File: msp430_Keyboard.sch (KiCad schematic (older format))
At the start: 26 parts, among them J1 Conn_01x04_Male, SW14 L_Super, SW4 L_Ctrl, SW48 R_Ctrl, SW5 L_Shift, SW53 R_Shift, SW57 Alt_GR, SW60 R_Super, SW61 FUNC, SW9 L_Alt, U1 MSP430F5510IRGZ, Y1 12MHz, Y2 32.768kHz

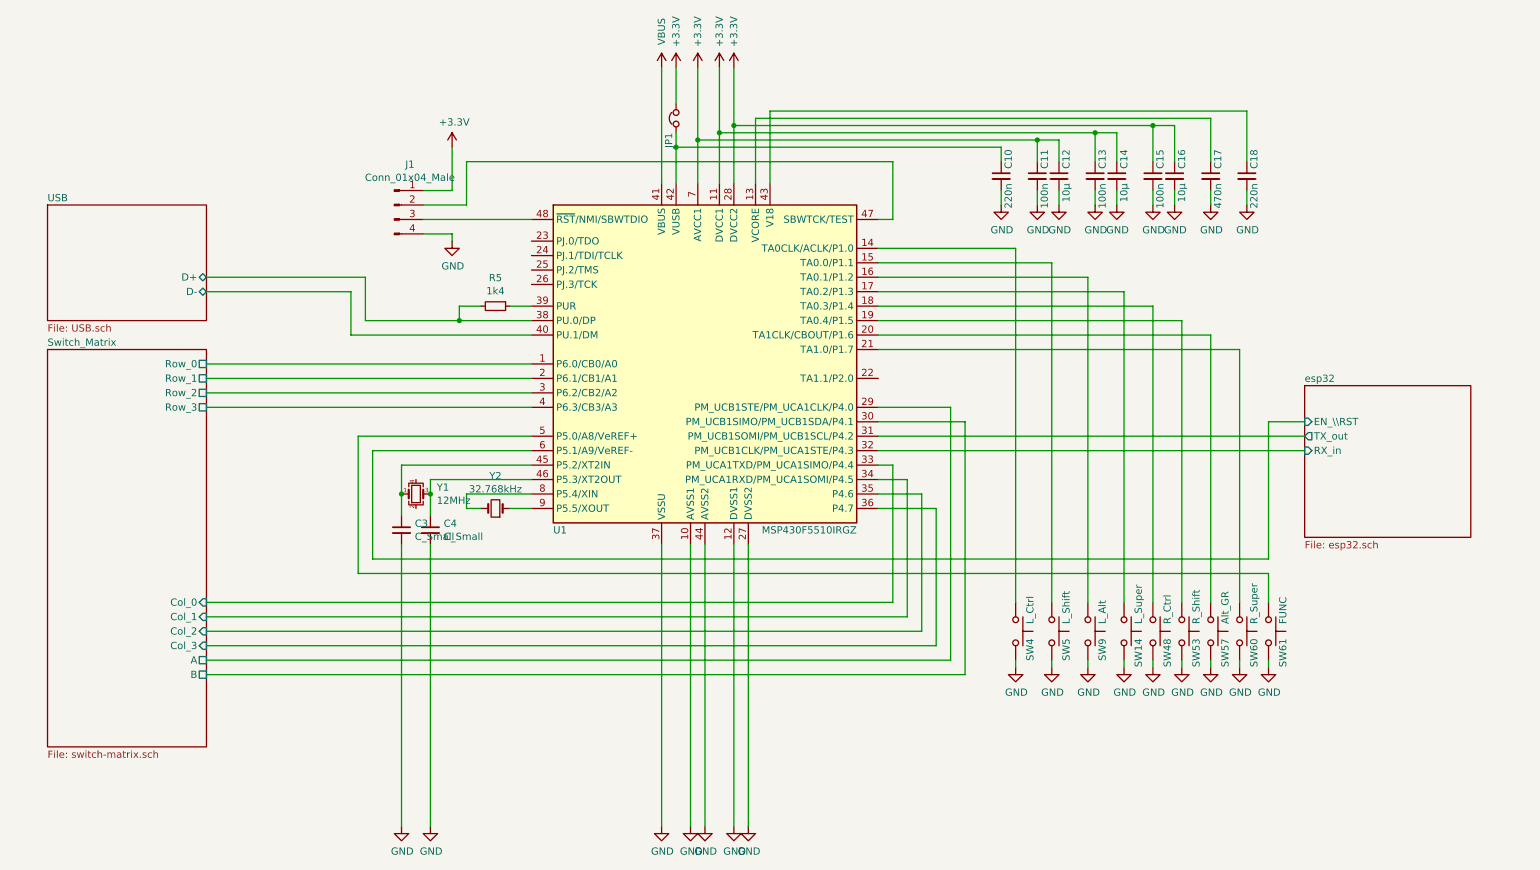
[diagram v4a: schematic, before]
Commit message: Layout sent to JLCPCB
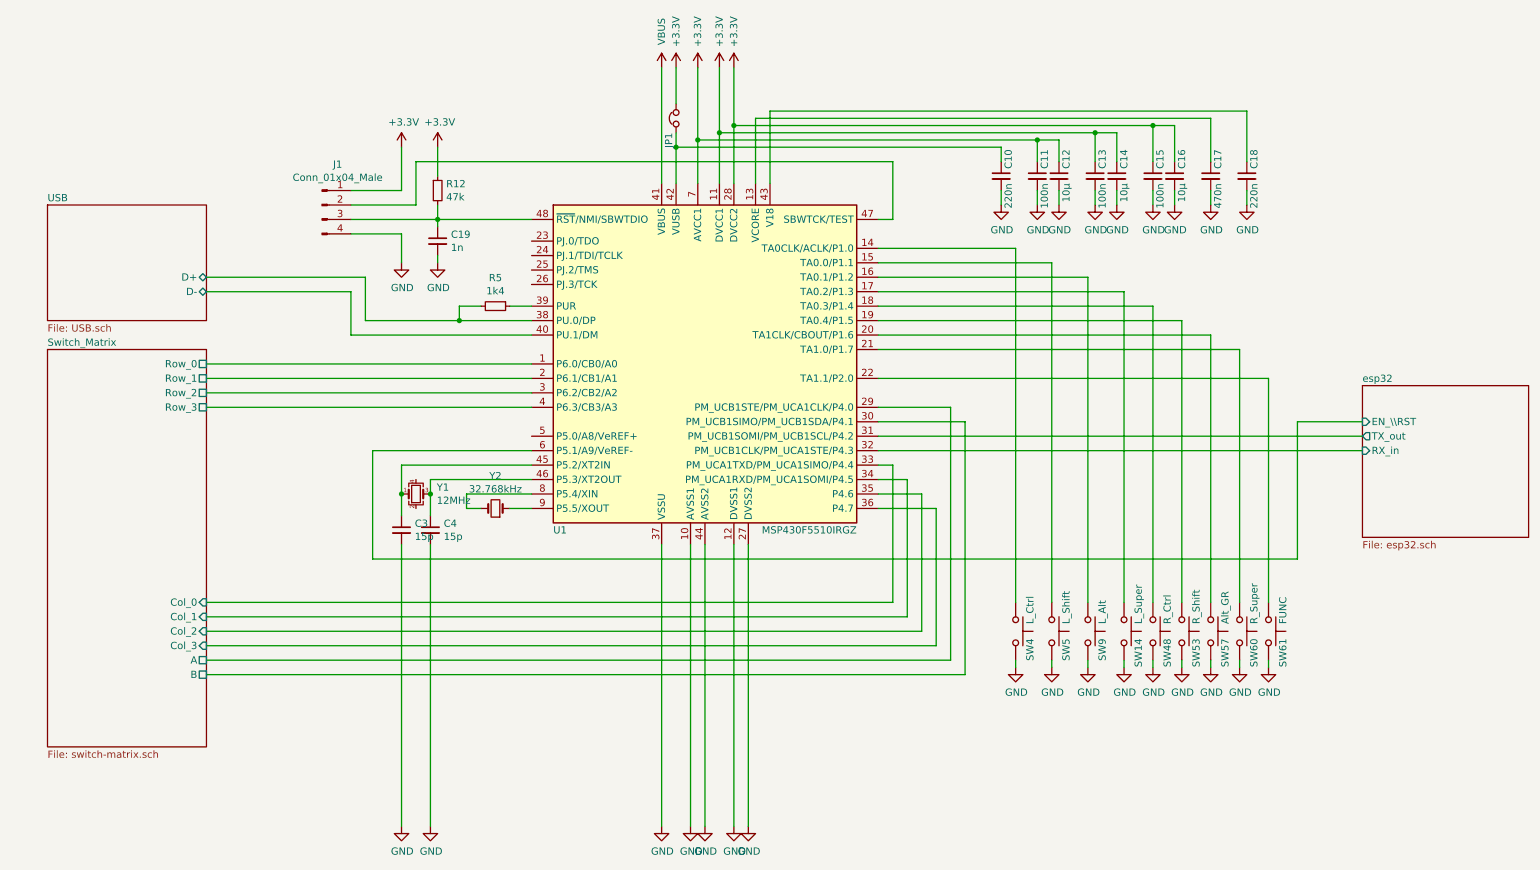
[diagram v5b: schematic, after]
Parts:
- added C19: 1n, Capacitor_SMD:C_0603_1608Metric_Pad1.08x0.95mm_HandSolder, symbol Device:C_Small
- added R12: 47k, Resistor_SMD:R_0603_1608Metric_Pad0.98x0.95mm_HandSolder, symbol Device:R_Small
- C3, C4: value C_Small -> 15p; footprint Capacitor_SMD:C_0603_1608Metric -> Capacitor_SMD:C_0603_1608Metric_Pad1.08x0.95mm_HandSolder
- R5: footprint Resistor_SMD:R_0603_1608Metric -> Resistor_SMD:R_0603_1608Metric_Pad0.98x0.95mm_HandSolder
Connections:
- net +3V3: now also R12.1
- net GND: now also C19.2
- net at U1.22 (TA1.1/P2.0): now also SW61.1
- net at J1.3 (Pin_3), U1.48 (~RST~/NMI/SBWTDIO): now also C19.1, R12.2
- net at U1.5 (P5.0/A8/VeREF+): no longer SW61.1
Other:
- moved on the sheet: J1
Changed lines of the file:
@@
 P 3350 4600
 F 0 "C3" H 3442 4646 50  0000 L CNN
-F 1 "C_Small" H 3442 4555 50  0000 L CNN
-F 2 "Capacitor_SMD:C_0603_1608Metric" H 3350 4600 50  0001 C CNN
+F 1 "15p" H 3442 4555 50  0000 L CNN
+F 2 "Capacitor_SMD:C_0603_1608Metric_Pad1.08x0.95mm_HandSolder" H 3350 4600 50  0001 C CNN
 F 3 "~" H 3350 4600 50  0001 C CNN
 	1    3350 4600
@@
 P 3550 4600
 F 0 "C4" H 3642 4646 50  0000 L CNN
-F 1 "C_Small" H 3642 4555 50  0000 L CNN
-F 2 "Capacitor_SMD:C_0603_1608Metric" H 3550 4600 50  0001 C CNN
+F 1 "15p" H 3642 4555 50  0000 L CNN
+F 2 "Capacitor_SMD:C_0603_1608Metric_Pad1.08x0.95mm_HandSolder" H 3550 4600 50  0001 C CNN
 F 3 "~" H 3550 4600 50  0001 C CNN
 	1    3550 4600
@@
 F 0 "R5" V 3804 3050 50  0000 C CNN
 F 1 "1k4" V 3895 3050 50  0000 C CNN
-F 2 "Resistor_SMD:R_0603_1608Metric" H 4000 3050 50  0001 C CNN
+F 2 "Resistor_SMD:R_0603_1608Metric_Pad0.98x0.95mm_HandSolder" H 4000 3050 50  0001 C CNN
 F 3 "~" H 4000 3050 50  0001 C CNN
 	1    4000 3050
@@
 L Connector:Conn_01x04_Male J1
 U 1 1 60C87E06
-P 3300 2350
-F 0 "J1" H 3408 2631 50  0000 C CNN
-F 1 "Conn_01x04_Male" H 3408 2540 50  0000 C CNN
-F 2 "Connector_PinHeader_1.27mm:PinHeader_1x04_P1.27mm_Horizontal" H 3300 2350 50  0001 C CNN
-F 3 "~" H 3300 2350 50  0001 C CNN
-	1    3300 2350
-	1    0    0    -1
-$EndComp
-Wire Wire Line
-	3500 2450 4250 2450
+P 2800 2350
+F 0 "J1" H 2908 2631 50  0000 C CNN
+F 1 "Conn_01x04_Male" H 2908 2540 50  0000 C CNN
+F 2 "Connector_PinHeader_1.27mm:PinHeader_1x04_P1.27mm_Horizontal" H 2800 2350 50  0001 C CNN
+F 3 "~" H 2800 2350 50  0001 C CNN
+	1    2800 2350
+	1    0    0    -1
+$EndComp
+Wire Wire Line
+	3000 2450 3600 2450
 $Comp
 L power:GND #PWR0114
 U 1 1 60C8AB36
-P 3700 2600
-F 0 "#PWR0114" H 3700 2350 50  0001 C CNN
-F 1 "GND" H 3705 2427 50  0000 C CNN
-F 2 "" H 3700 2600 50  0001 C CNN
-F 3 "" H 3700 2600 50  0001 C CNN
-	1    3700 2600
-	1    0    0    -1
-$EndComp
-Wire Wire Line
-	3700 2600 3700 2550
-Wire Wire Line
-	3700 2550 3500 2550
-Wire Wire Line
-	3500 2350 3800 2350
-Wire Wire Line
-	3800 2350 3800 2050
-Wire Wire Line
-	3800 2050 6750 2050
+P 3350 2750
+F 0 "#PWR0114" H 3350 2500 50  0001 C CNN
+F 1 "GND" H 3355 2577 50  0000 C CNN
+F 2 "" H 3350 2750 50  0001 C CNN
+F 3 "" H 3350 2750 50  0001 C CNN
+	1    3350 2750
+	1    0    0    -1
+$EndComp
+Wire Wire Line
+	3350 2750 3350 2550
+Wire Wire Line
+	3350 2550 3000 2550
+Wire Wire Line
+	3000 2350 3450 2350
+Wire Wire Line
+	3450 2350 3450 2050
+Wire Wire Line
+	3450 2050 6750 2050
 Wire Wire Line
 	6750 2050 6750 2450
@@
 L power:+3.3V #PWR0115
 U 1 1 60C98CCE
-P 3700 1950
-F 0 "#PWR0115" H 3700 1800 50  0001 C CNN
-F 1 "+3.3V" H 3715 2123 50  0000 C CNN
-F 2 "" H 3700 1950 50  0001 C CNN
-F 3 "" H 3700 1950 50  0001 C CNN
-	1    3700 1950
-	1    0    0    -1
-$EndComp
-Wire Wire Line
-	3700 1950 3700 2250
-Wire Wire Line
-	3700 2250 3500 2250
+P 3350 1950
+F 0 "#PWR0115" H 3350 1800 50  0001 C CNN
+F 1 "+3.3V" H 3365 2123 50  0000 C CNN
+F 2 "" H 3350 1950 50  0001 C CNN
+F 3 "" H 3350 1950 50  0001 C CNN
+	1    3350 1950
+	1    0    0    -1
+$EndComp
+Wire Wire Line
+	3350 1950 3350 2250
+Wire Wire Line
+	3350 2250 3000 2250
 $Comp
 L power:VBUS #PWR0116
@@
 	3550 4350 3550 4500
 Wire Wire Line
-	4250 3950 3050 3950
-Wire Wire Line
-	3050 3950 3050 4900
-Wire Wire Line
 	4250 4050 3150 4050
 Wire Wire Line
 	3150 4050 3150 4800
 Wire Wire Line
-	9350 4900 9350 5100
-Wire Wire Line
-	3050 4900 9350 4900
-Wire Wire Line
-	9350 3850 9350 4800
-Wire Wire Line
-	3150 4800 9350 4800
-Wire Wire Line
-	9600 3850 9350 3850
+	9550 3850 9550 4800
+Wire Wire Line
+	3150 4800 9550 4800
+Wire Wire Line
+	10000 3850 9550 3850
 $Sheet
-S 9600 3600 1150 1050
+S 10000 3600 1150 1050
 U 60CACA0F
 F0 "esp32" 50
 F1 "esp32.sch" 50
-F2 "EN_\\RST" I L 9600 3850 50
-F3 "TX_out" O L 9600 3950 50
-F4 "RX_in" I L 9600 4050 50
+F2 "EN_\\RST" I L 10000 3850 50
+F3 "TX_out" O L 10000 3950 50
+F4 "RX_in" I L 10000 4050 50
 $EndSheet
 Wire Wire Line
-	9600 3950 6650 3950
-Wire Wire Line
-	6650 4050 9600 4050
+	10000 3950 6650 3950
+Wire Wire Line
+	6650 4050 10000 4050
 Wire Wire Line
 	7250 5600 7250 3850
@@
 Wire Wire Line
 	5550 1850 8150 1850
+Wire Wire Line
+	6650 3550 9350 3550
+Wire Wire Line
+	9350 3550 9350 5100
+$Comp
+L Device:R_Small R12
+U 1 1 610C3A39
+P 3600 2250
+F 0 "R12" H 3659 2296 50  0000 L CNN
+F 1 "47k" H 3659 2205 50  0000 L CNN
+F 2 "Resistor_SMD:R_0603_1608Metric_Pad0.98x0.95mm_HandSolder" H 3600 2250 50  0001 C CNN
+F 3 "~" H 3600 2250 50  0001 C CNN
+	1    3600 2250
+	1    0    0    -1
+$EndComp
+$Comp
+L Device:C_Small C19
+U 1 1 610C4A02
+P 3600 2600
+F 0 "C19" H 3692 2646 50  0000 L CNN
+F 1 "1n" H 3692 2555 50  0000 L CNN
+F 2 "Capacitor_SMD:C_0603_1608Metric_Pad1.08x0.95mm_HandSolder" H 3600 2600 50  0001 C CNN
+F 3 "~" H 3600 2600 50  0001 C CNN
+	1    3600 2600
+	1    0    0    -1
+$EndComp
+$Comp
+L power:GND #PWR035
+U 1 1 610D83E9
+P 3600 2750
+F 0 "#PWR035" H 3600 2500 50  0001 C CNN
+F 1 "GND" H 3605 2577 50  0000 C CNN
+F 2 "" H 3600 2750 50  0001 C CNN
+F 3 "" H 3600 2750 50  0001 C CNN
+	1    3600 2750
+	1    0    0    -1
+$EndComp
+$Comp
+L power:+3.3V #PWR034
+U 1 1 610D8AD1
+P 3600 1950
+F 0 "#PWR034" H 3600 1800 50  0001 C CNN
+F 1 "+3.3V" H 3615 2123 50  0000 C CNN
+F 2 "" H 3600 1950 50  0001 C CNN
+F 3 "" H 3600 1950 50  0001 C CNN
+	1    3600 1950
+	1    0    0    -1
+$EndComp
+Wire Wire Line
+	3600 1950 3600 2150
+Wire Wire Line
+	3600 2700 3600 2750
+Wire Wire Line
+	3600 2350 3600 2450
+Connection ~ 3600 2450
+Wire Wire Line
+	3600 2450 4250 2450
+Wire Wire Line
+	3600 2500 3600 2450
 $EndSCHEMATC

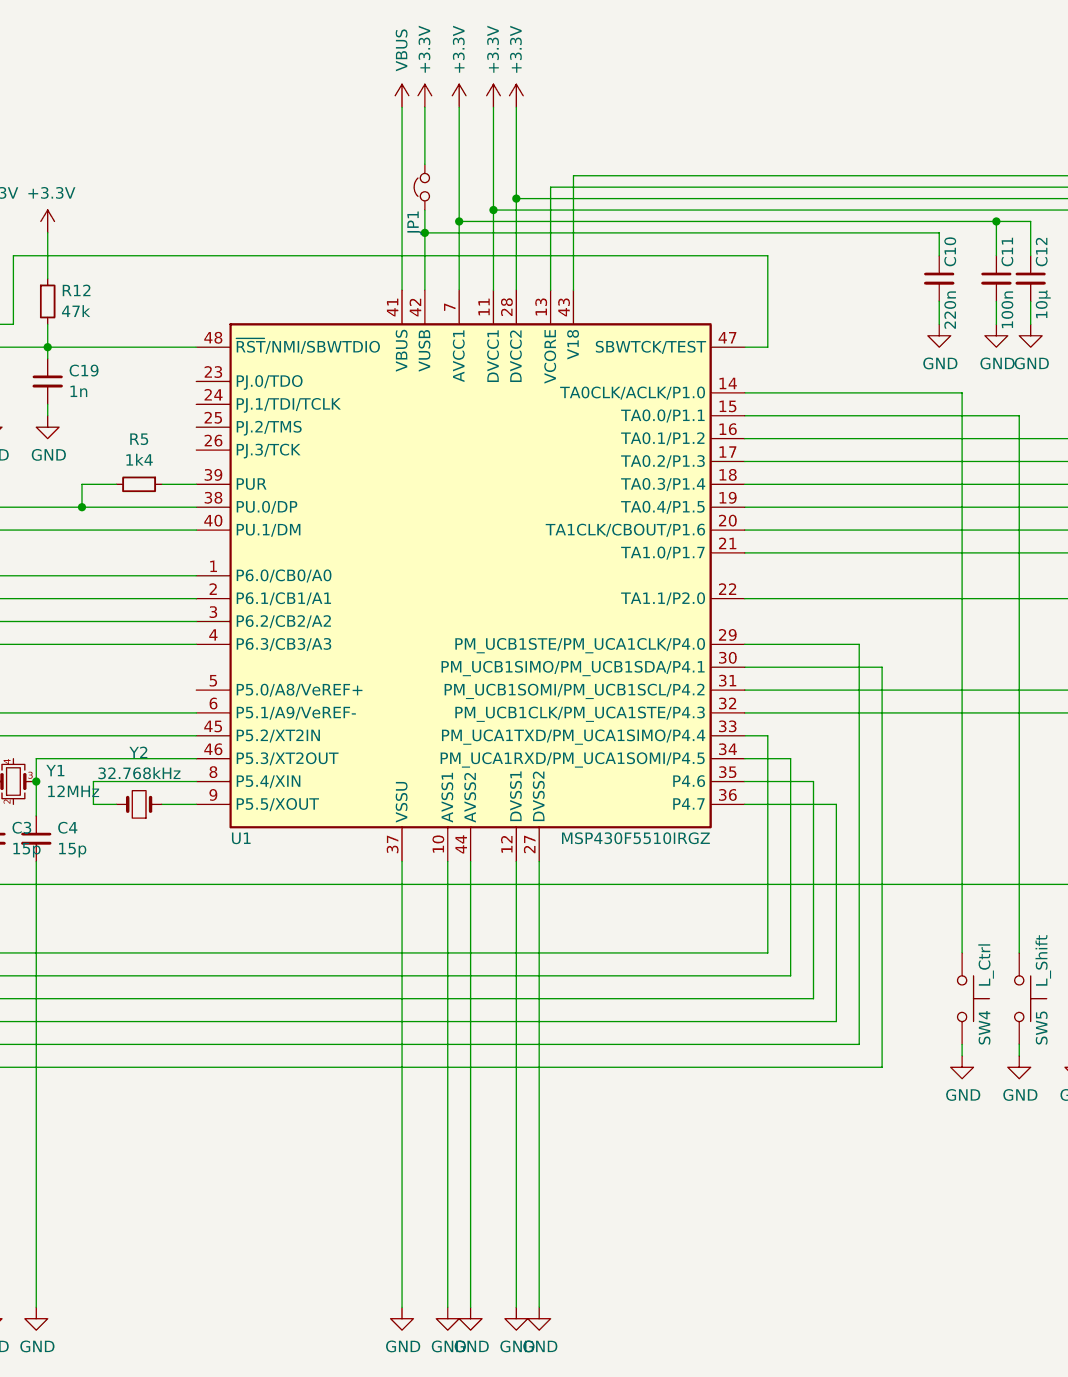
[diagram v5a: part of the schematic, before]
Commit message: Filterung in den USB-Leitungen, VBus besser abgeblockt, Enter Taste gedreht
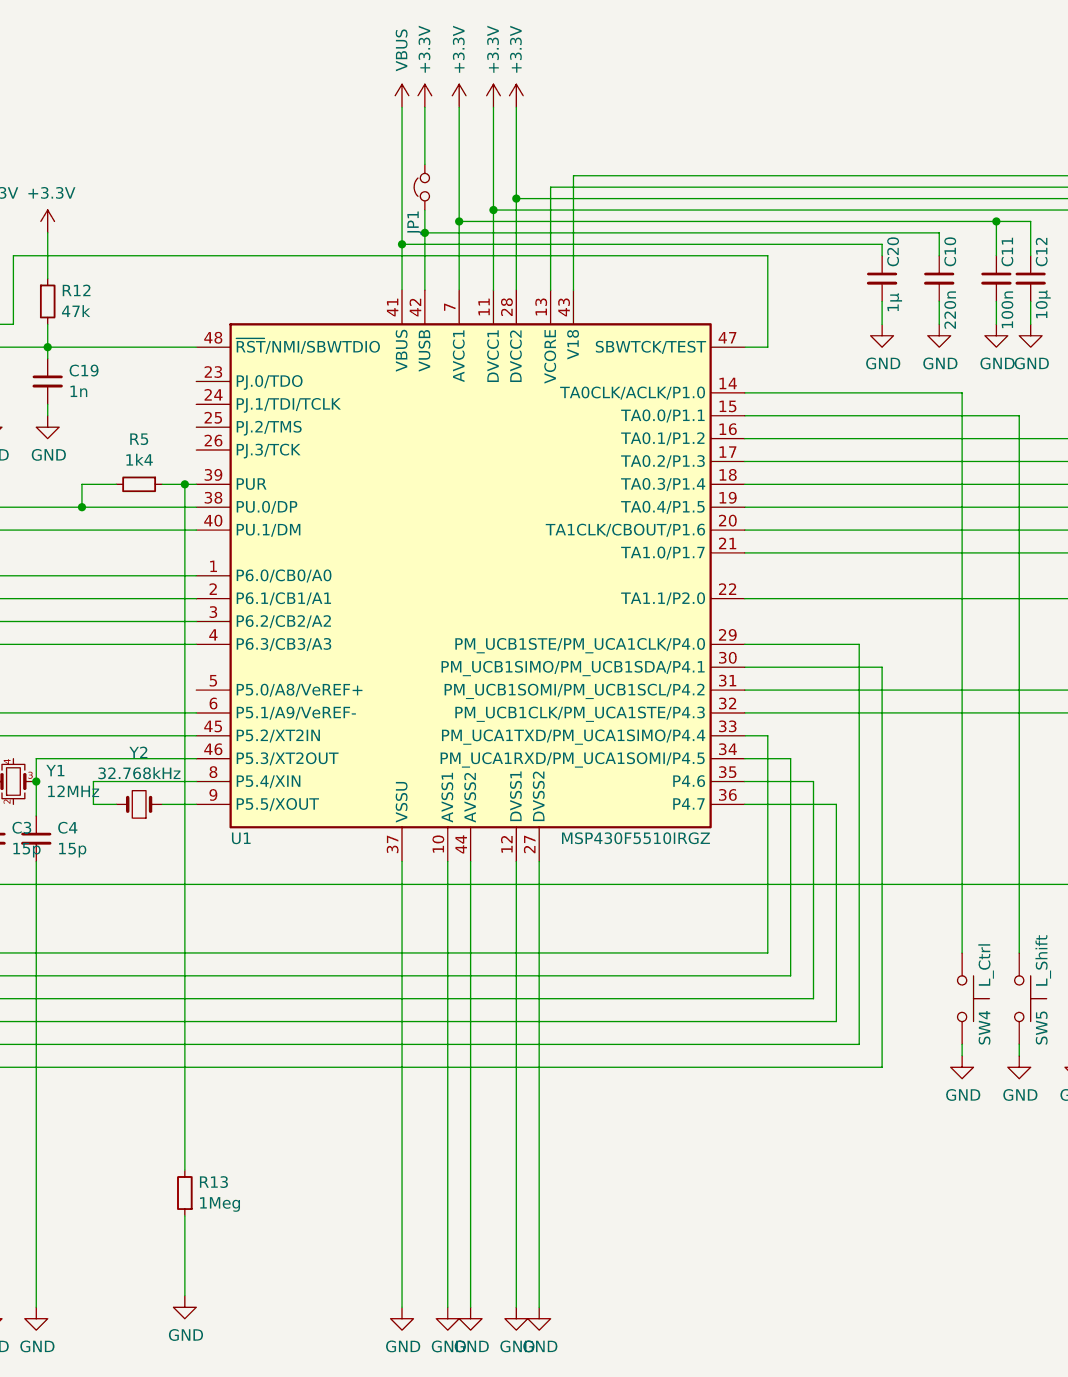
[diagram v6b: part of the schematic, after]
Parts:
- added C20: 1μ, Capacitor_SMD:C_0603_1608Metric_Pad1.08x0.95mm_HandSolder, symbol Device:C_Small
- added R13: 1Meg, Resistor_SMD:R_0603_1608Metric_Pad0.98x0.95mm_HandSolder, symbol Device:R_Small
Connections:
- net GND: now also C20.2, R13.1
- net VBUS: now also C20.1
- net at R5.1, U1.39 (PUR): now also R13.2
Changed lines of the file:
@@
 $EndComp
 Wire Wire Line
-	4250 3050 4100 3050
+	4250 3050 4200 3050
 Wire Wire Line
 	3900 3050 3750 3050
@@
 	8700 1800 8700 2050
 Wire Wire Line
-	5150 1400 5150 2200
+	5150 1400 5150 2000
 Wire Wire Line
 	8950 2050 8950 1750
@@
 Wire Wire Line
 	3600 2500 3600 2450
+$Comp
+L Device:R_Small R13
+U 1 1 6111513C
+P 4200 6150
+F 0 "R13" H 4141 6104 50  0000 R CNN
+F 1 "1Meg" H 4141 6195 50  0000 R CNN
+F 2 "Resistor_SMD:R_0603_1608Metric_Pad0.98x0.95mm_HandSolder" H 4200 6150 50  0001 C CNN
+F 3 "~" H 4200 6150 50  0001 C CNN
+	1    4200 6150
+	-1   0    0    1
+$EndComp
+$Comp
+L power:GND #PWR036
+U 1 1 6111D6CF
+P 4200 6600
+F 0 "#PWR036" H 4200 6350 50  0001 C CNN
+F 1 "GND" H 4205 6427 50  0000 C CNN
+F 2 "" H 4200 6600 50  0001 C CNN
+F 3 "" H 4200 6600 50  0001 C CNN
+	1    4200 6600
+	1    0    0    -1
+$EndComp
+Wire Wire Line
+	4200 6600 4200 6250
+Wire Wire Line
+	4200 6050 4200 3050
+Connection ~ 4200 3050
+Wire Wire Line
+	4200 3050 4100 3050
+$Comp
+L Device:C_Small C20
+U 1 1 611F5392
+P 7250 2150
+F 0 "C20" V 7300 2200 50  0000 L CNN
+F 1 "1μ" V 7300 2000 50  0000 L CNN
+F 2 "Capacitor_SMD:C_0603_1608Metric_Pad1.08x0.95mm_HandSolder" H 7250 2150 50  0001 C CNN
+F 3 "~" H 7250 2150 50  0001 C CNN
+	1    7250 2150
+	1    0    0    -1
+$EndComp
+$Comp
+L power:GND #PWR037
+U 1 1 611F5913
+P 7250 2350
+F 0 "#PWR037" H 7250 2100 50  0001 C CNN
+F 1 "GND" H 7255 2177 50  0000 C CNN
+F 2 "" H 7250 2350 50  0001 C CNN
+F 3 "" H 7250 2350 50  0001 C CNN
+	1    7250 2350
+	1    0    0    -1
+$EndComp
+Wire Wire Line
+	7250 2350 7250 2250
+Wire Wire Line
+	7250 2050 7250 2000
+Wire Wire Line
+	7250 2000 5150 2000
+Connection ~ 5150 2000
+Wire Wire Line
+	5150 2000 5150 2200
 $EndSCHEMATC
